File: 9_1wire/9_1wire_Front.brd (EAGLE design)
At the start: 71.5 x 24 mm, 2 parts

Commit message: Cleanup, front with lib elements
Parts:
- removed E$1: (no value), AllSerialv2:RIA_AKL182-03
- removed E$2: (no value), AllSerialv2:PANEL
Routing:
- removed copper zone on layer 16, net S$2
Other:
- outline, holes or cut-outs redrawn
- board text added: "AllSerial 1wire"
- board text removed: "1wire"

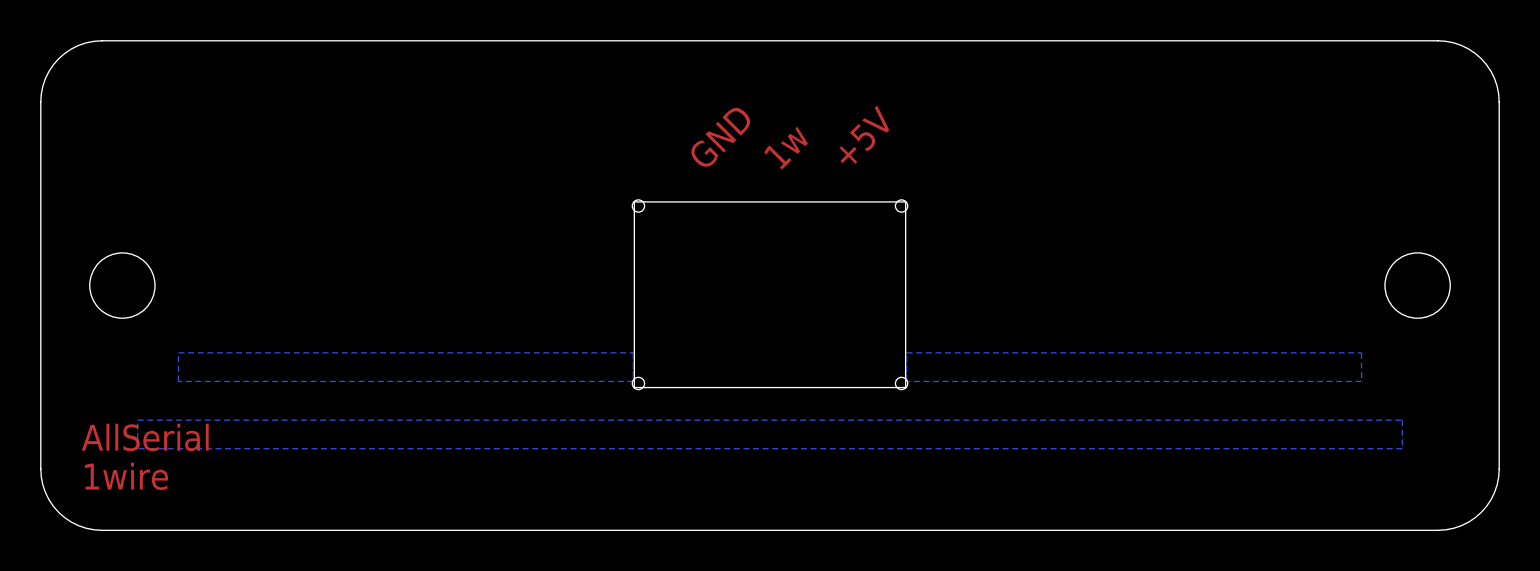
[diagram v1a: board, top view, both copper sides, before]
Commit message: pro mini layout corrected
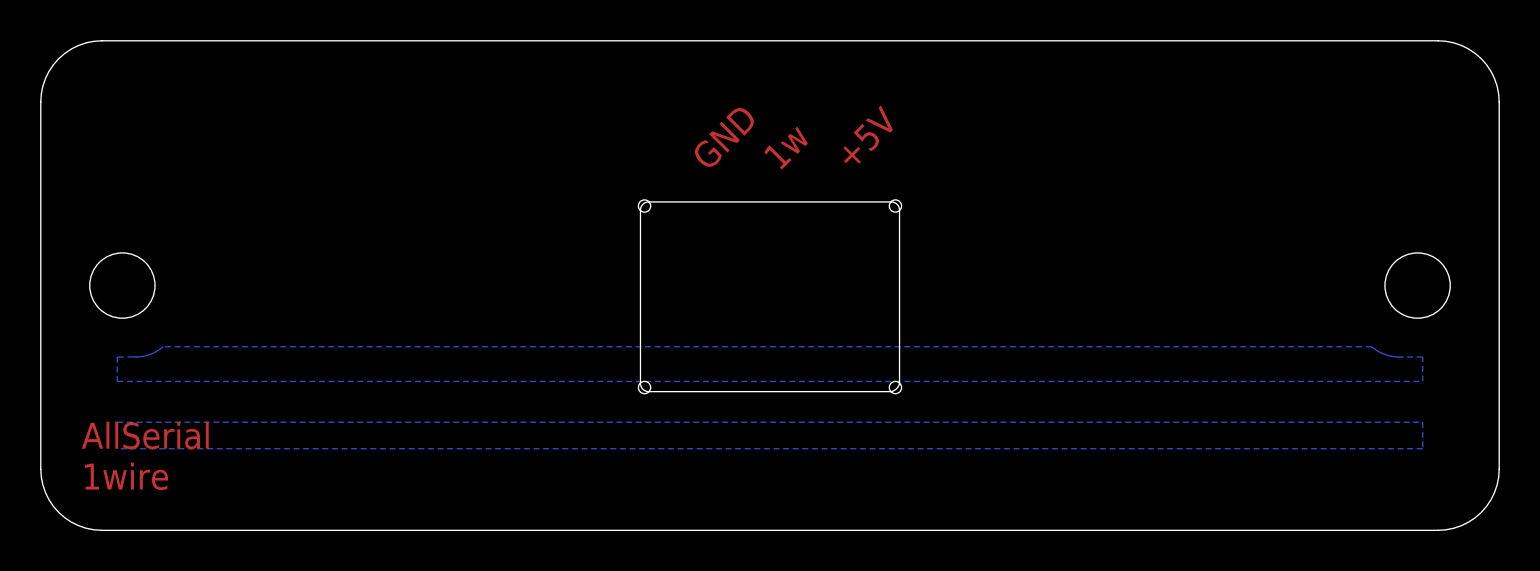
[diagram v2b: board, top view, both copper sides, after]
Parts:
- added E$1: (no value), AllSerialv2:RIA_AKL182-03
- added E$2: (no value), AllSerialv2:PANEL
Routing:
- added copper zone on layer 16, net S$2
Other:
- outline, holes or cut-outs redrawn
- board text added: "1wire"
- board text removed: "AllSerial 1wire"
